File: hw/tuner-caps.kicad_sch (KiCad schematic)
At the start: 47 parts, among them K7720 G5Q-14-05, K7721 G5Q-14-05, K7722 G5Q-14-05, K7723 G5Q-14-05, K7724 G5Q-14-05, K7725 G5Q-14-05, K7726 G5Q-14-05, K7727 G5Q-14-05, K7728 G5Q-14-05, K7729 G5Q-14-05, K7730 G5Q-14-05, K7731 G5Q-14-05, K7732 G5Q-14-05, K7733 G5Q-14-05, K7734 G5Q-14-05, K7735 G5Q-14-05, K7736 G5Q-14-05, K7737 G5Q-14-05, U7760 TPIC6C595PWR

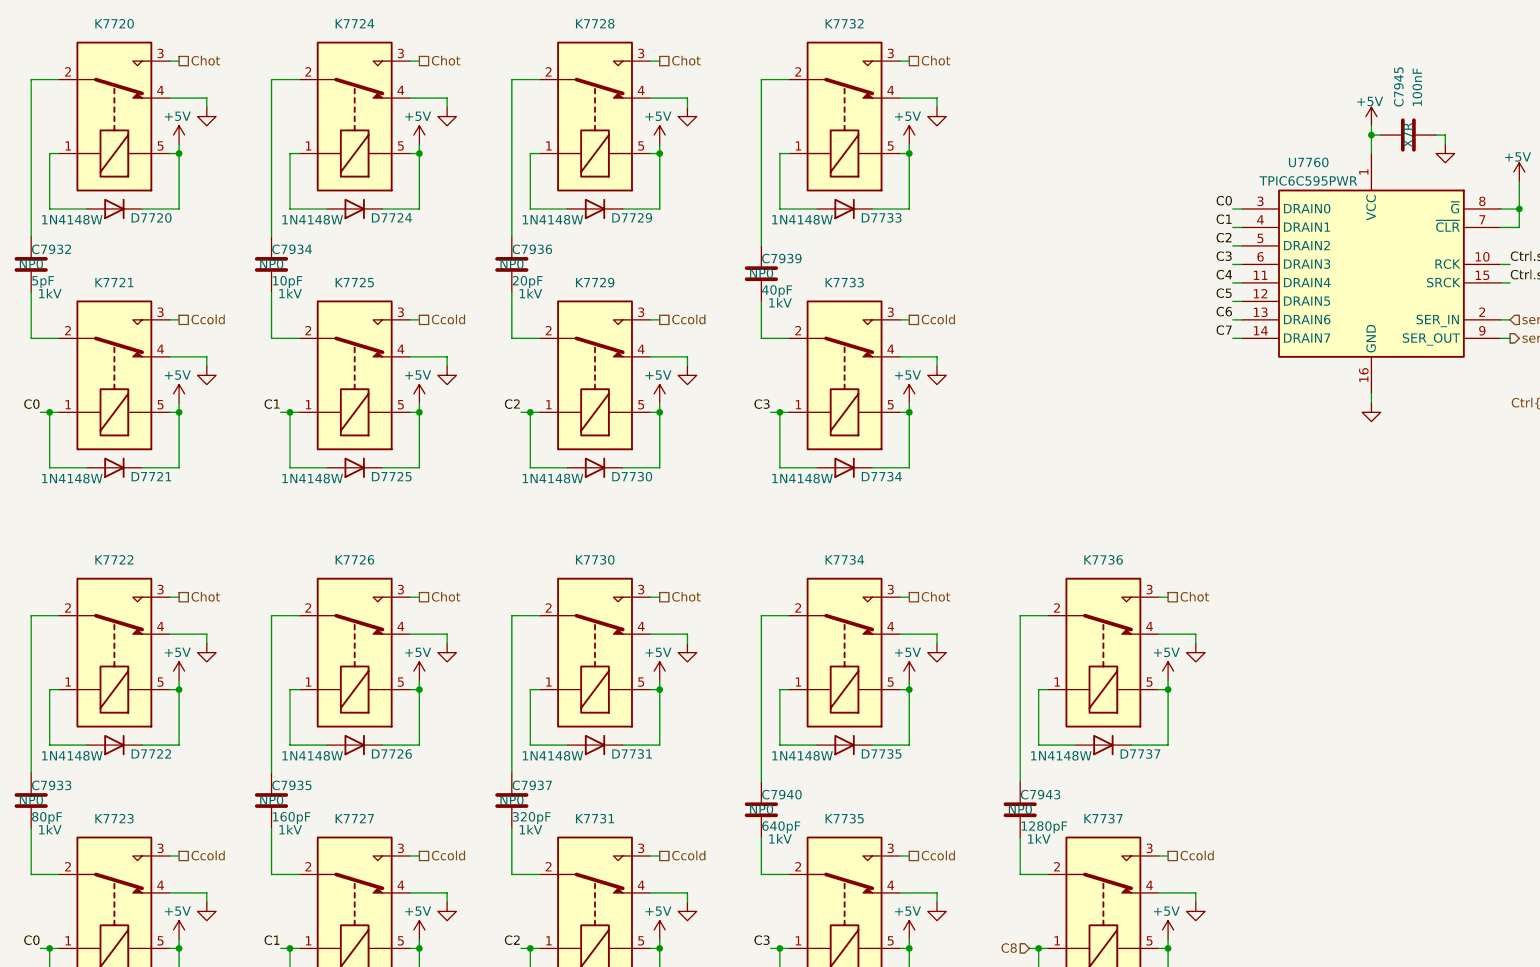
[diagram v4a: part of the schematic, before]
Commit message: OK I have part numbers for consolidated caps, resistors, inductors and all ICs are now Uxxx refdes.
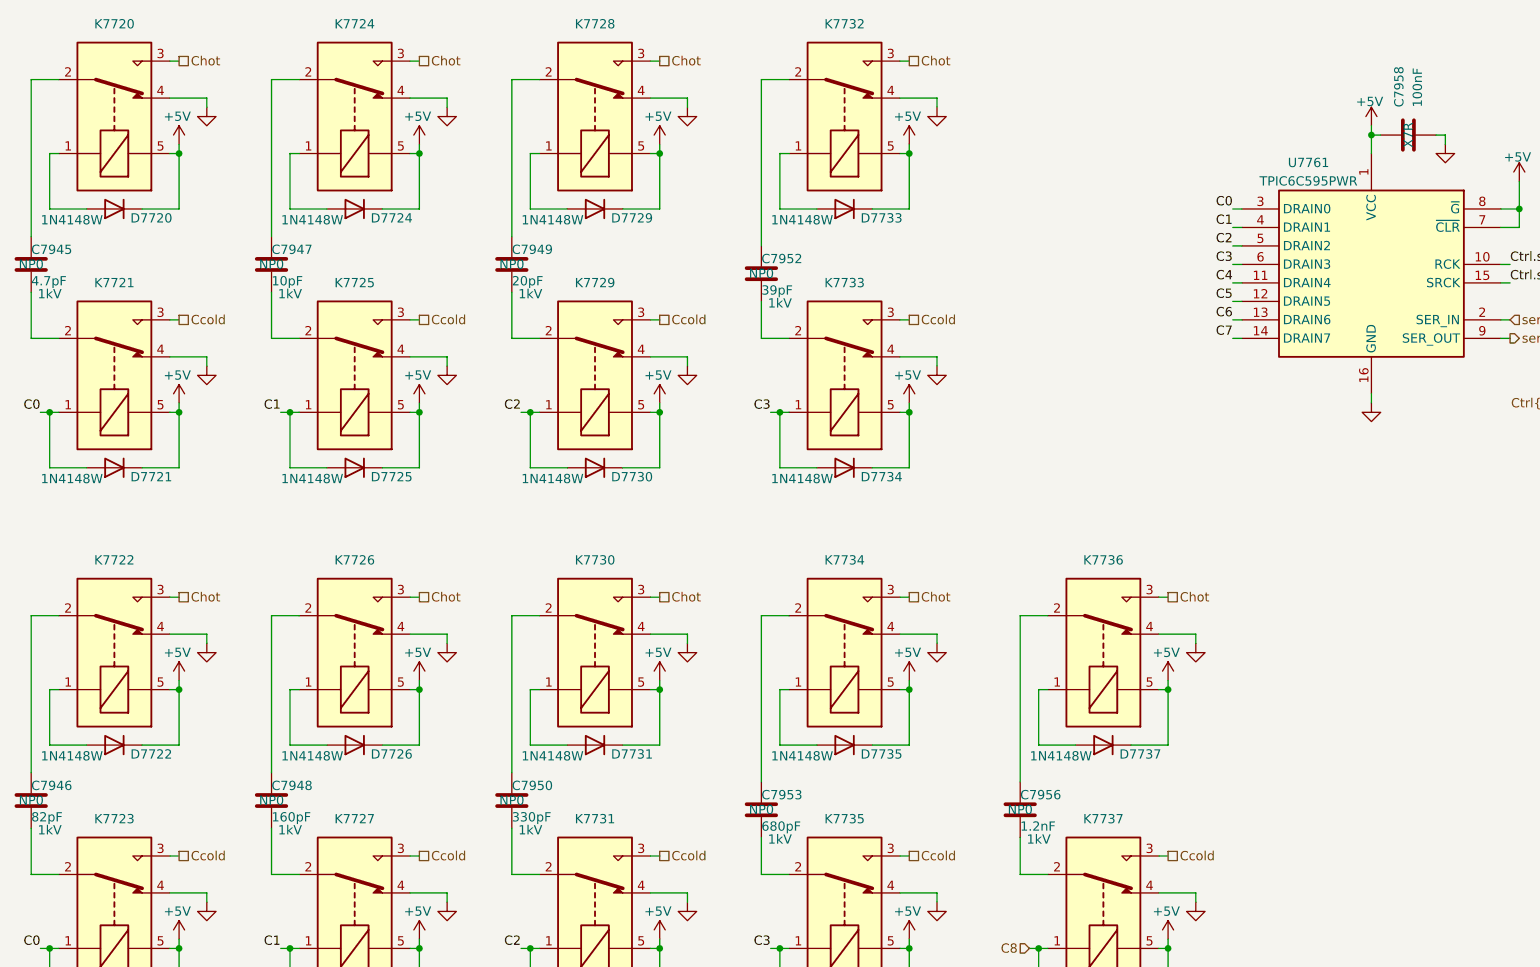
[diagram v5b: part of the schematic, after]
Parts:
- C7945: renamed from C7932; value 5pF -> 4.7pF; footprint Capacitor_SMD:C_0603_1608Metric -> Capacitor_SMD:C_0805_2012Metric; Manufacturer_Name (none) -> Knowles Syfer; Manufacturer_Part_Number (none) -> 0805Y1K04P70DCT; Mouser Part Number (none) -> 766-0805Y1K04P70DCT
- C7946: renamed from C7933; value 80pF -> 82pF; footprint Capacitor_SMD:C_0603_1608Metric -> Capacitor_SMD:C_0805_2012Metric; Manufacturer_Name (none) -> KEMET; Manufacturer_Part_Number (none) -> C0805C820JDGACTU; Mouser Part Number (none) -> 80-C0805C820JDG
- C7947: renamed from C7934; footprint Capacitor_SMD:C_0603_1608Metric -> Capacitor_SMD:C_1206_3216Metric; Manufacturer_Name (none) -> YAGEO; Manufacturer_Part_Number (none) -> CC0805JRNPOCBN100; Mouser Part Number (none) -> 603-CC0805JRNPOCBN10
- C7948: renamed from C7935; footprint Capacitor_SMD:C_0603_1608Metric -> Capacitor_SMD:C_0805_2012Metric; Manufacturer_Name (none) -> YAGEO; Manufacturer_Part_Number (none) -> C0805C161GDGACAUTO; Mouser Part Number (none) -> 80-C0805C161GDGACATO
- C7949: renamed from C7936; footprint Capacitor_SMD:C_0603_1608Metric -> Capacitor_SMD:C_1206_3216Metric; Manufacturer_Name (none) -> YAGEO; Manufacturer_Part_Number (none) -> CC1206JKNPOCBN200; Mouser Part Number (none) -> 603-CC1206JNPOCBN200
- C7950: renamed from C7937; value 320pF -> 330pF; footprint Capacitor_SMD:C_0603_1608Metric -> Capacitor_SMD:C_1206_3216Metric; Manufacturer_Name (none) -> YAGEO; Manufacturer_Part_Number (none) -> CC1206JKNPOCBN331; Mouser Part Number (none) -> 603-CC126JKNPOCBN331
- C7952: renamed from C7939; value 40pF -> 39pF; footprint Capacitor_SMD:C_0603_1608Metric -> Capacitor_SMD:C_1206_3216Metric; Manufacturer_Name (none) -> YAGEO; Manufacturer_Part_Number (none) -> CC1206JKNPOCBN390; Mouser Part Number (none) -> 603-CC1206JKCBN390
- C7953: renamed from C7940; value 640pF -> 680pF; footprint Capacitor_SMD:C_0603_1608Metric -> Capacitor_SMD:C_1206_3216Metric; Manufacturer_Name (none) -> YAGEO; Manufacturer_Part_Number (none) -> CC1206JKNPOCBN681; Mouser Part Number (none) -> 603-CC126JKNPOCBN681
- C7956: renamed from C7943; value 1280pF -> 1.2nF; footprint Capacitor_SMD:C_0603_1608Metric -> Capacitor_SMD:C_1210_3225Metric; Manufacturer_Name (none) -> TDK; Manufacturer_Part_Number (none) -> CGA6M1C0G3A122J200AC; Mouser Part Number (none) -> 810-CGA6M1C0G3A1J2A
- C7958: renamed from C7945; Manufacturer_Name (none) -> Kemet; Manufacturer_Part_Number (none) -> C0805F104K1RACAUTO; Mouser Part Number (none) -> 80-C0805F104K1RAUTO; working-voltage 10V -> 50V
- renumbered U7760 to U7761

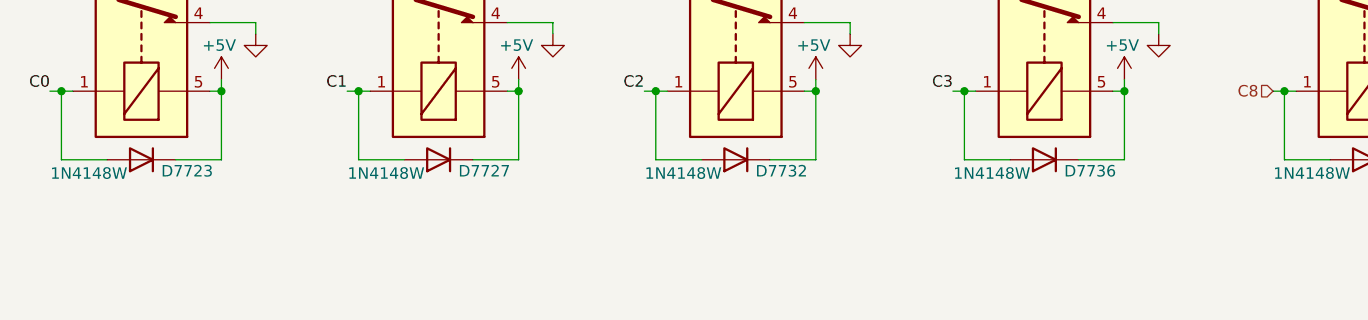
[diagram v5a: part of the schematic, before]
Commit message: Clean up some footprints no longer used. Build footprints for LPF and antenna tuner inductors.
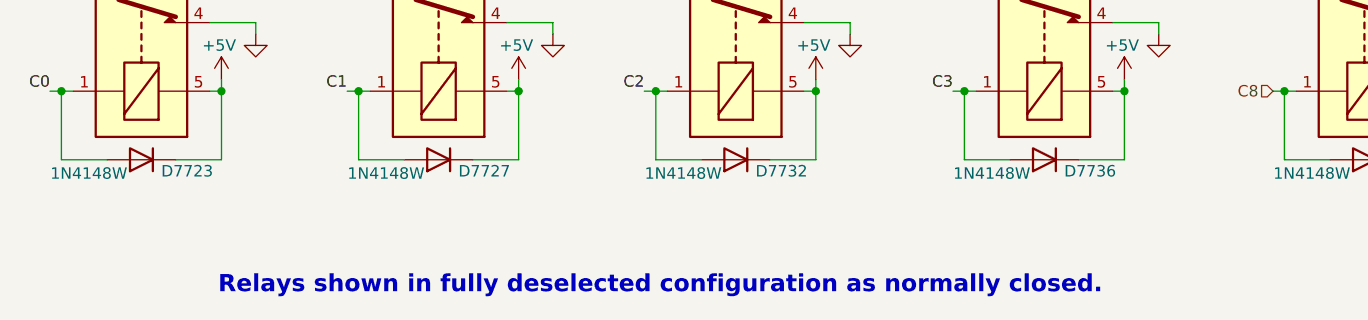
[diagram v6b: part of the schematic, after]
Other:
- note added: "Relays shown in fully deselected configuration as normally closed."
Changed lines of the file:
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@@
 		(comment 1 "Alan Mimms")
+	)
+	(text "Relays shown in fully deselected configuration as normally closed."
+		(exclude_from_sim no)
+		(at 88.138 165.1 0)
+		(effects
+			(font
+				(size 1.905 1.905)
+				(thickness 0.381)
+				(bold yes)
+			)
+		)
 	)
 	(junction

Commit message: All symbols and footprints seem right now, and schematic again imports into PCB without error
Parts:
- renumbered C7945 to C7944, C7946 to C7945, C7947 to C7946, C7948 to C7947, C7949 to C7948, C7950 to C7949, C7952 to C7951, C7953 to C7952, C7956 to C7955, C7958 to C7957, U7761 to U7760

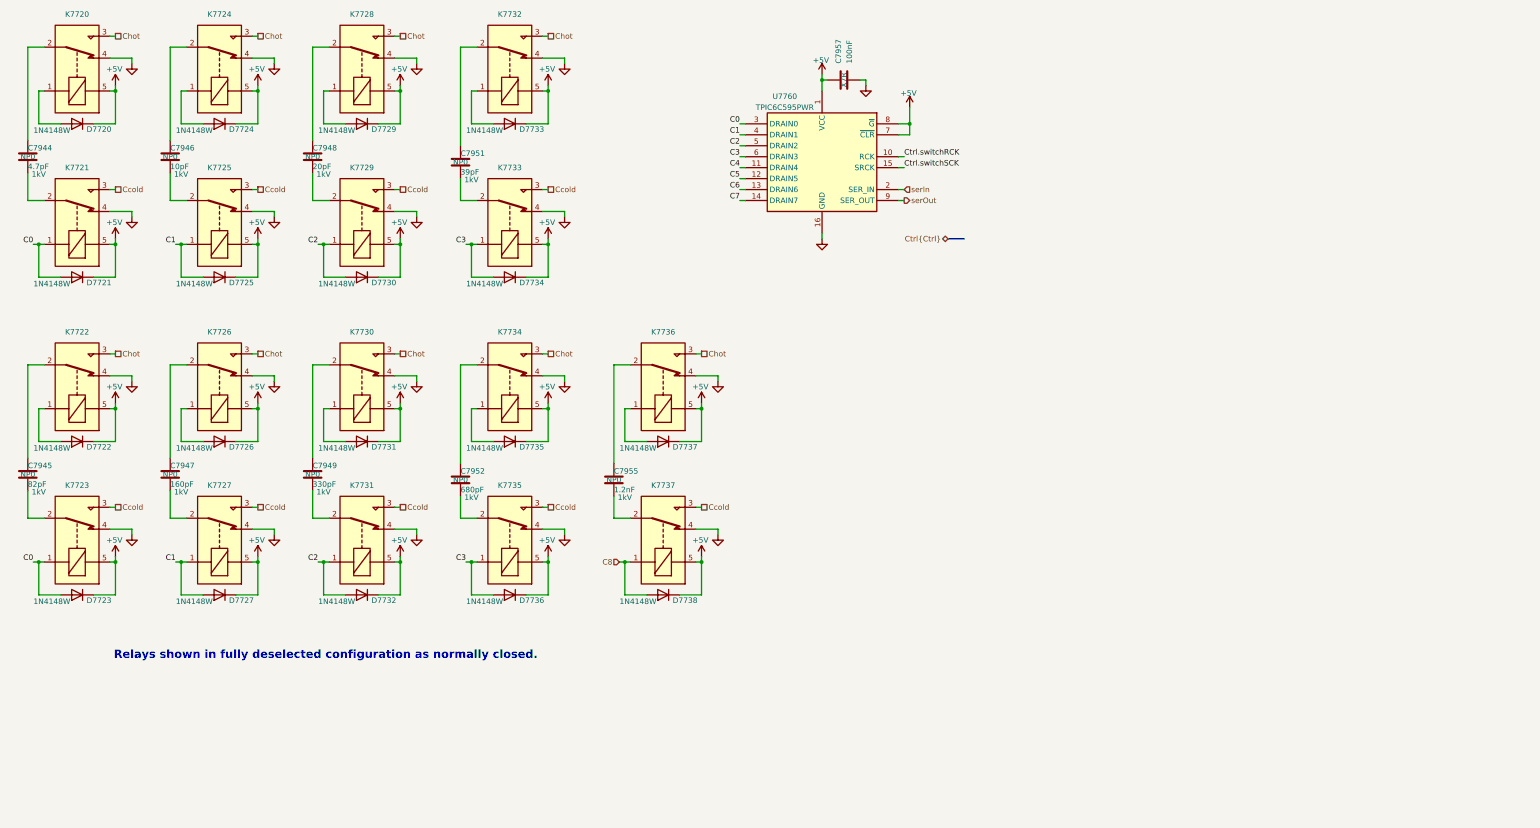
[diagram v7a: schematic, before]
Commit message: About to switch to series-L + shunt-C fore/aft PI network config for antenna tuner
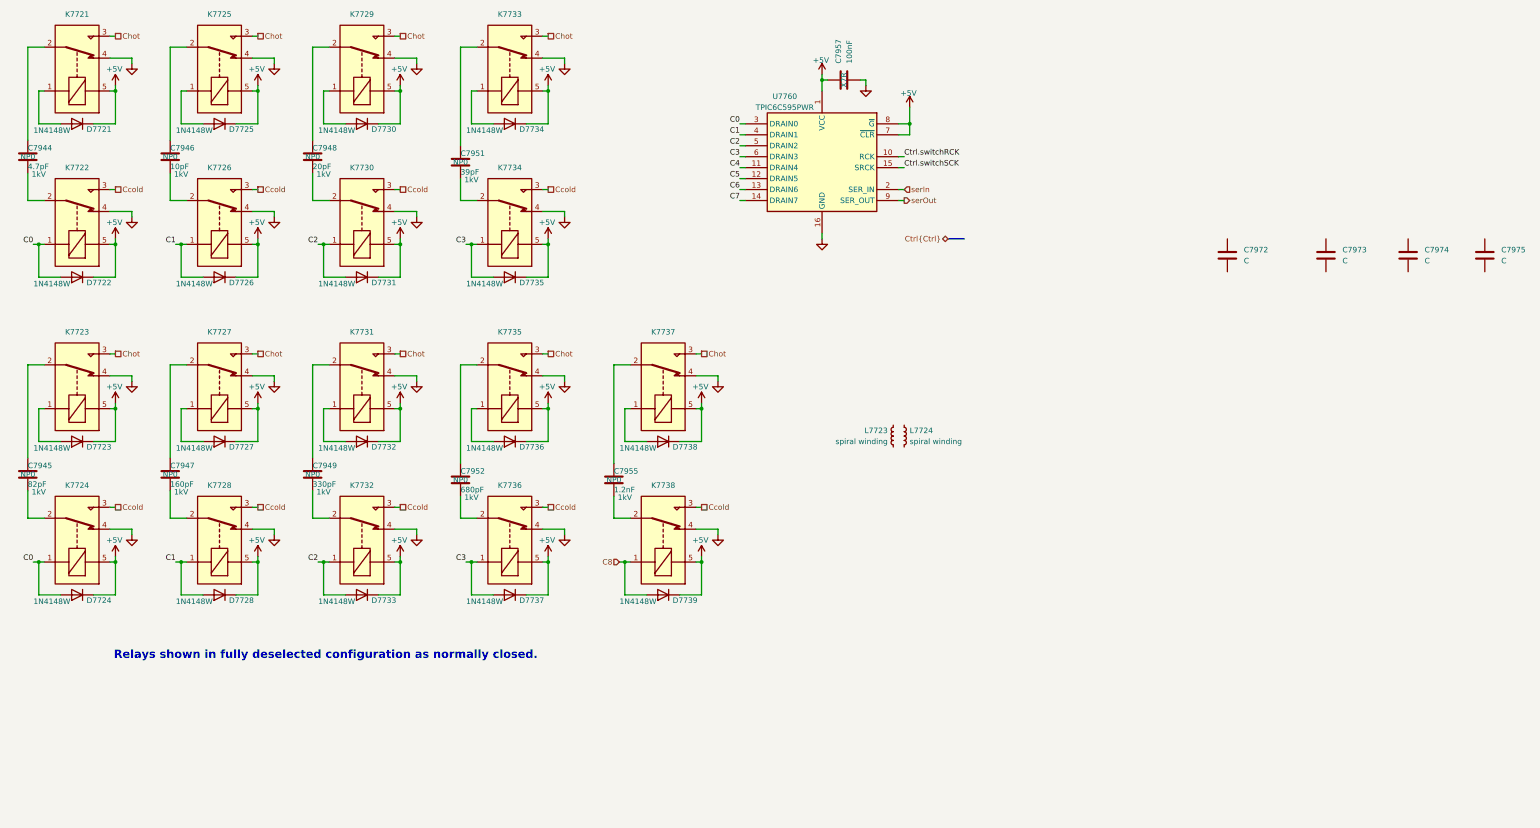
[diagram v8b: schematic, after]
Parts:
- added C7972, C7973, C7974, C7975: C, symbol Device:C
- added L7723, L7724: spiral winding, symbol Device:L_Small
- renumbered D7720 to D7721, D7721 to D7722, D7722 to D7723, D7723 to D7724, D7724 to D7725, D7725 to D7726, D7726 to D7727, D7727 to D7728, D7729 to D7730, D7730 to D7731, D7731 to D7732, D7732 to D7733, D7733 to D7734, D7734 to D7735, D7735 to D7736, D7736 to D7737, D7737 to D7738, D7738 to D7739, K7720 to K7721, K7721 to K7722, K7722 to K7723, K7723 to K7724, K7724 to K7725, K7725 to K7726, K7726 to K7727, K7727 to K7728, K7728 to K7729, K7729 to K7730, K7730 to K7731, K7731 to K7732, K7732 to K7733, K7733 to K7734, K7734 to K7735, K7735 to K7736, K7736 to K7737, K7737 to K7738
